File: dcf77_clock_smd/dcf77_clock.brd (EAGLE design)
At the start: 83.5 x 76.2 mm, 42 parts, among them IC1 7805DT, IC2 ATMEGA48/88/168-AU, J2 DCJ0202, Q1 32.768kHz, Q2 IRLML6244TRPBF, SW1 EC12E_SW, U1 LCD-16X2SILK, U2 DS1307SO8

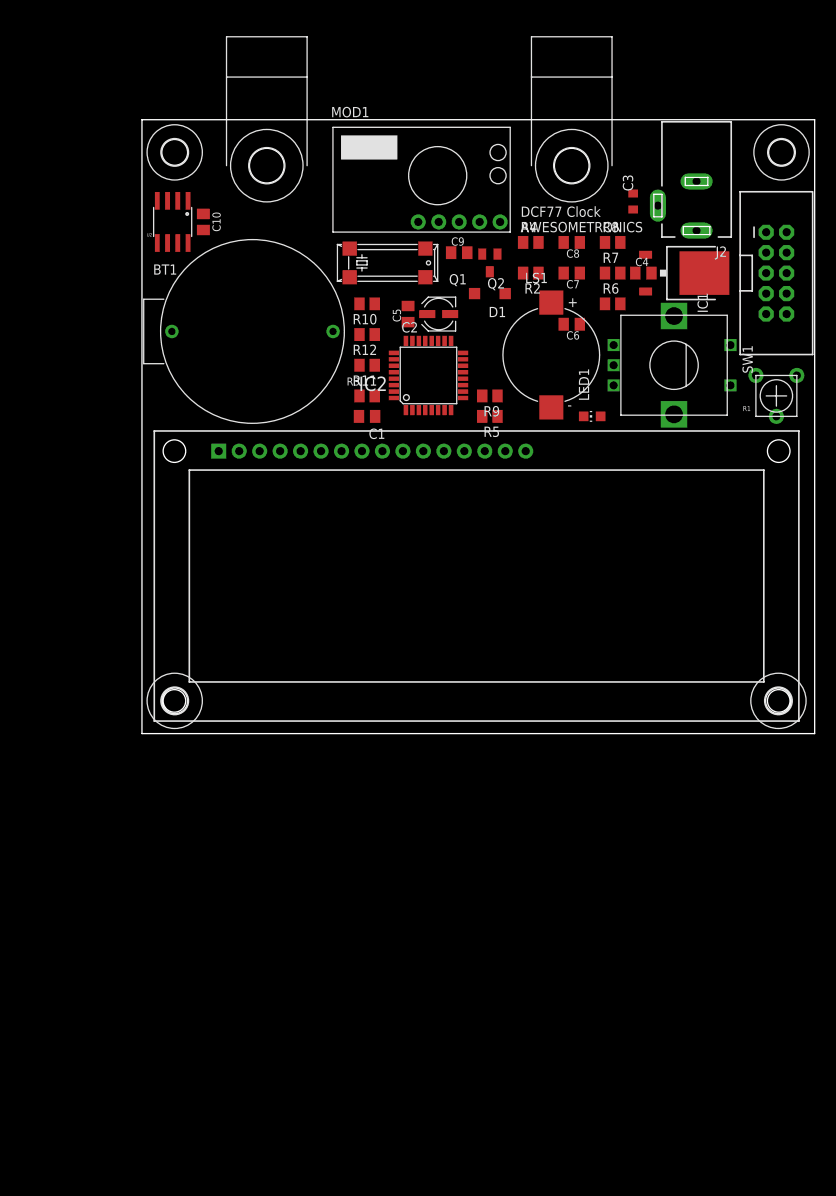
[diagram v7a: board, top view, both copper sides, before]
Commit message: Allign mounting holes
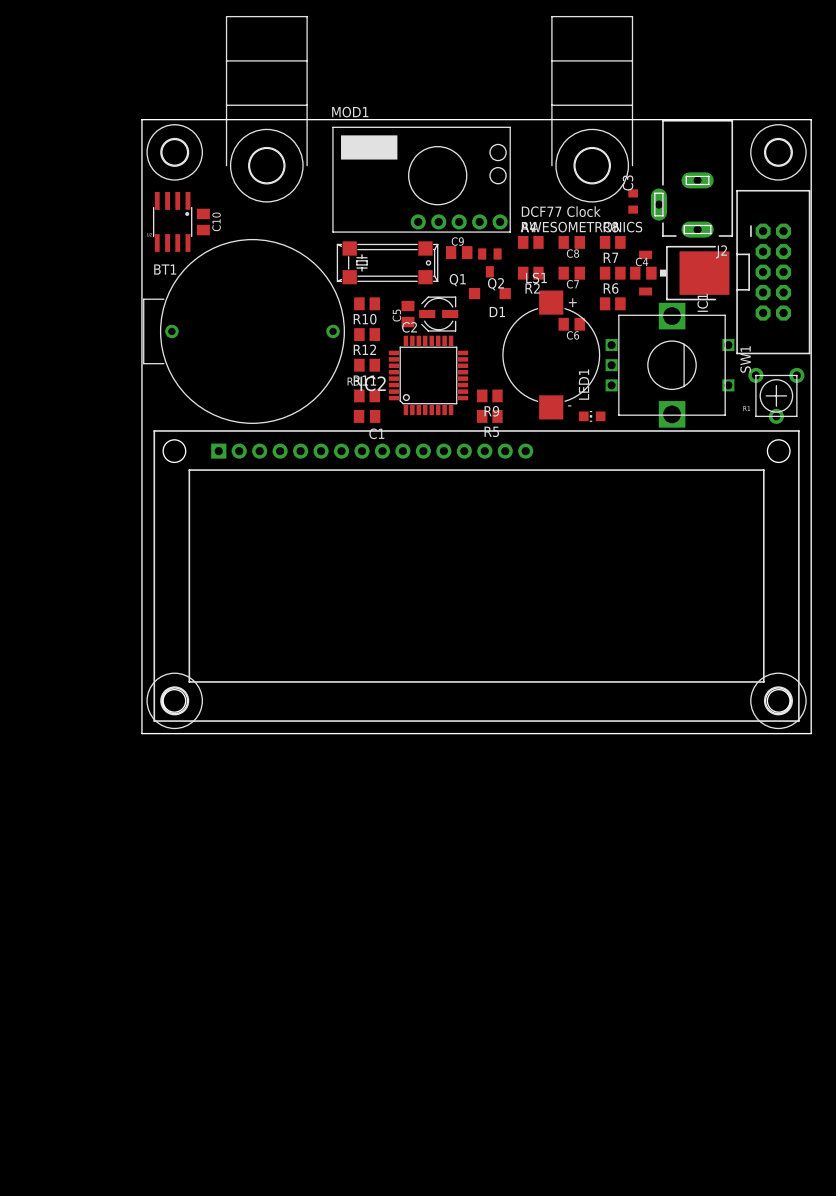
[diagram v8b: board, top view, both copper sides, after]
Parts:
- HOLD1, HOLD2: value COREHOLDER -> COREHOLDERH6P; device dcf77:H5P -> dcf77:H6P
- moved HOLD2 2.54 mm to (55.9, 70.5)
- moved U$1 0.40 mm to (78.4, 57.3)
- moved H4 0.38 mm to (79.0, 72.1)
- moved SW1 0.25 mm to (65.8, 45.7)
- moved J2 0.18 mm to (69.0, 65.7)
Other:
- board size 83.5 x 76.2 mm -> 83.1 x 76.2 mm
